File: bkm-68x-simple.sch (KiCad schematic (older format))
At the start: 0 parts

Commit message: Fixes and additions
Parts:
- added H1, H2: SCREWMOUNT_90DEG, keystone-7794:7794-X, symbol Mechanical:MountingHole
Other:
- note added: "MECHANICAL"
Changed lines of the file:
@@
 F1 "fpga.sch" 60
 $EndSheet
+Wire Notes Line
+	850  6000 3050 6000
+Wire Notes Line
+	3050 6000 3050 4550
+Wire Notes Line
+	3050 4550 850  4550
+Wire Notes Line
+	850  4550 850  6000
+Text Notes 1700 4500 0    50   ~ 0
+MECHANICAL
+$Comp
+L Mechanical:MountingHole H1
+U 1 1 60AB1DD9
+P 1150 4900
+F 0 "H1" H 1250 4946 50  0000 L CNN
+F 1 "SCREWMOUNT_90DEG" H 1250 4855 50  0000 L CNN
+F 2 "keystone-7794:7794-X" H 1150 4900 50  0001 C CNN
+F 3 "~" H 1150 4900 50  0001 C CNN
+	1    1150 4900
+	1    0    0    -1
+$EndComp
+$Comp
+L Mechanical:MountingHole H2
+U 1 1 60AB2057
+P 1150 5600
+F 0 "H2" H 1250 5646 50  0000 L CNN
+F 1 "SCREWMOUNT_90DEG" H 1250 5555 50  0000 L CNN
+F 2 "keystone-7794:7794-X" H 1150 5600 50  0001 C CNN
+F 3 "~" H 1150 5600 50  0001 C CNN
+	1    1150 5600
+	1    0    0    -1
+$EndComp
 $EndSCHEMATC

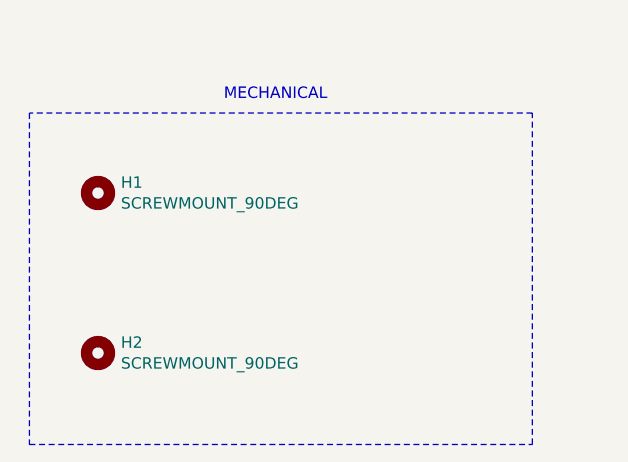
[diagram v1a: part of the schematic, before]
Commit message: Name screw mount part, add licence
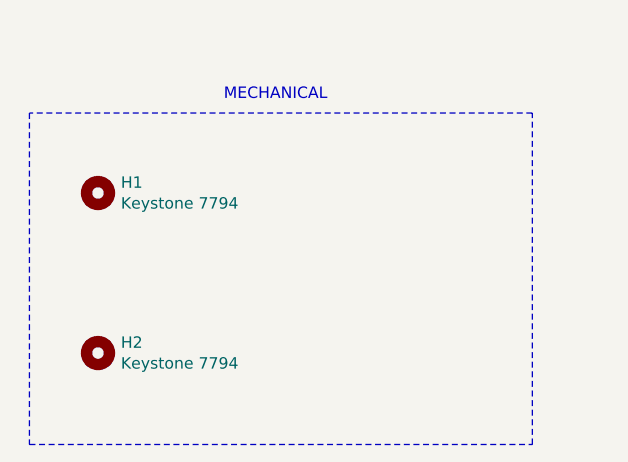
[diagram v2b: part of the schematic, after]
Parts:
- H1, H2: value SCREWMOUNT_90DEG -> Keystone 7794
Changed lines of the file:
@@
 P 1150 4900
 F 0 "H1" H 1250 4946 50  0000 L CNN
-F 1 "SCREWMOUNT_90DEG" H 1250 4855 50  0000 L CNN
+F 1 "Keystone 7794" H 1250 4855 50  0000 L CNN
 F 2 "keystone-7794:7794-X" H 1150 4900 50  0001 C CNN
 F 3 "~" H 1150 4900 50  0001 C CNN
@@
 P 1150 5600
 F 0 "H2" H 1250 5646 50  0000 L CNN
-F 1 "SCREWMOUNT_90DEG" H 1250 5555 50  0000 L CNN
+F 1 "Keystone 7794" H 1250 5555 50  0000 L CNN
 F 2 "keystone-7794:7794-X" H 1150 5600 50  0001 C CNN
 F 3 "~" H 1150 5600 50  0001 C CNN
